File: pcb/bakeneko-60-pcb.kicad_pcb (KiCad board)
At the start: 2 copper layers, 284.7 x 94.2 mm, 147 parts, among them J1 JST SH 4-pin, J2 AVR-ISP-6, SW1 Reset, U1 SRV05-4, U2 ATmega32U4-AU, Y1 16MHz

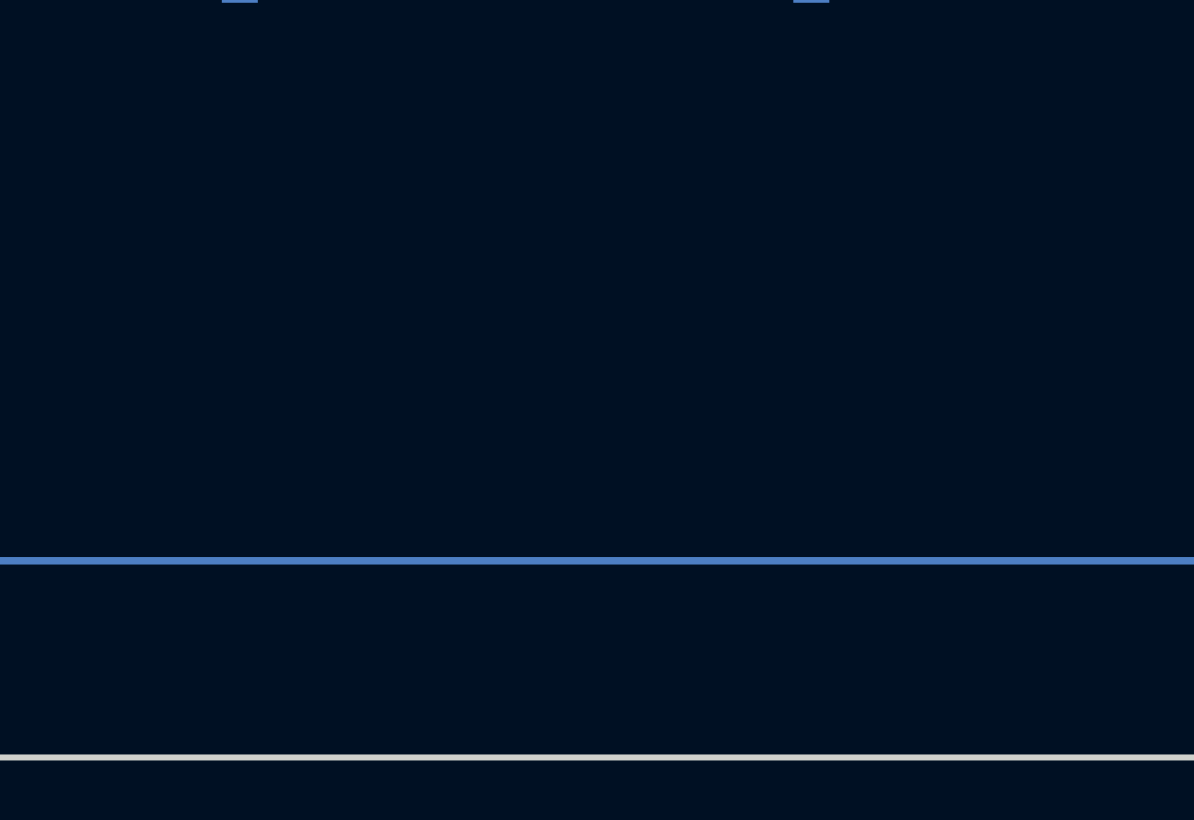
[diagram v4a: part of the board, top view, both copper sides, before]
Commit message: Place right 2.25 spacebar
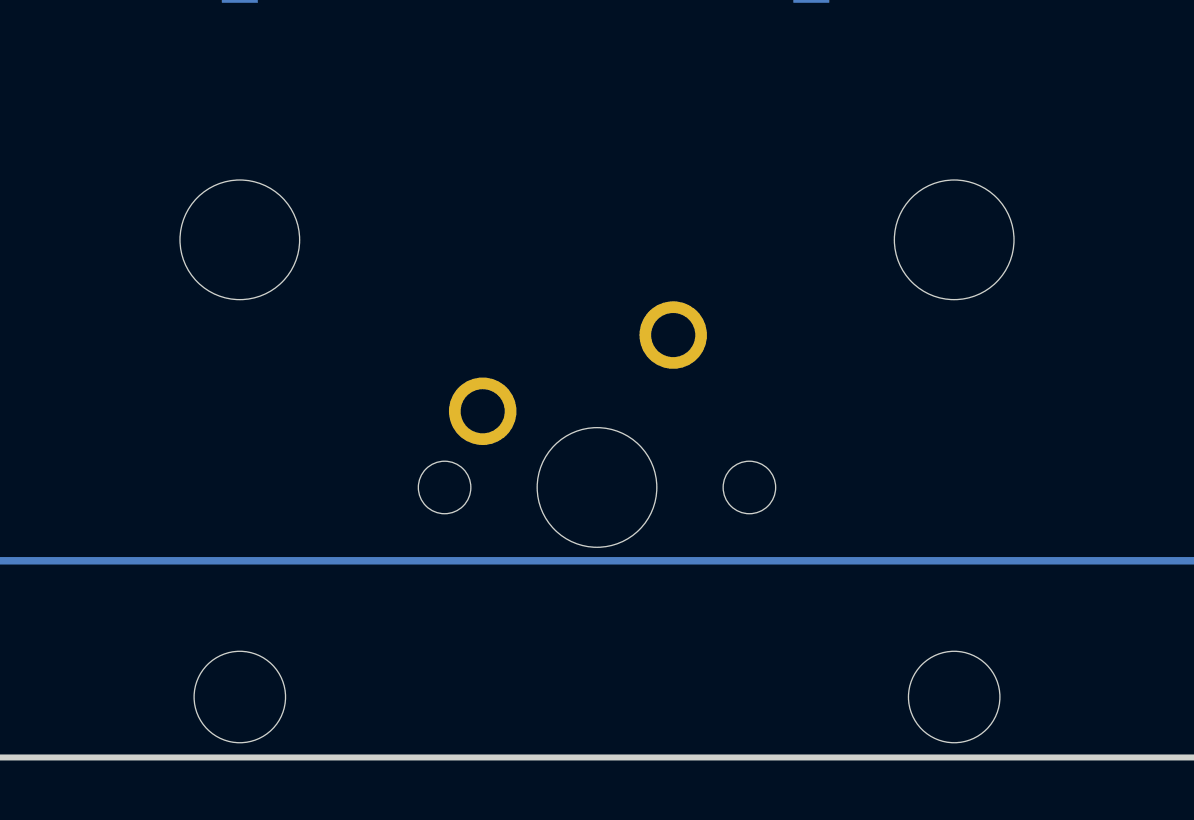
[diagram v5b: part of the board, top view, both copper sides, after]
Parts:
- added MX67: 2.25U, MX_Only:MXOnly-2.25U-ReversedStabilizers-NoLED, F.Cu at (168.5, 85.2)
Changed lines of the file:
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@@
       (net 91 "COL13"))
-  )
-  (footprint "MX_Only:MXOnly-2.25U-ReversedStabilizers-NoLED" (layer "F.Cu")
-    (at 92.34375 85.2)
-    (attr through_hole)
-    (fp_text reference "MX66" (at 0 3.175) (layer "Dwgs.User")
-      (effects (font (size 1 1) (thickness 0.15)))
-    )
-    (fp_text value "2.25U" (at 0 -7.9375) (layer "Dwgs.User")
-      (effects (font (size 1 1) (thickness 0.15)))
-    )
-    (fp_line (start 7 -7) (end 7 -5) (layer "Dwgs.User") (width 0.15))
-    (fp_line (start -7 -7) (end -7 -5) (layer "Dwgs.User") (width 0.15))
-    (fp_line (start 21.43125 -9.525) (end 21.43125 9.525) (layer "Dwgs.User") (width 0.15))
-    (fp_line (start -21.43125 9.525) (end -21.43125 -9.525) (layer "Dwgs.User") (width 0.15))
-    (fp_line (start 5 7) (end 7 7) (layer "Dwgs.User") (width 0.15))
-    (fp_line (start 7 7) (end 7 5) (layer "Dwgs.User") (width 0.15))
-    (fp_line (start -7 7) (end -5 7) (layer "Dwgs.User") (width 0.15))
-    (fp_line (start -21.43125 9.525) (end 21.43125 9.525) (layer "Dwgs.User") (width 0.15))
-    (fp_line (start -21.43125 -9.525) (end 21.43125 -9.525) (layer "Dwgs.User") (width 0.15))
-    (fp_line (start -7 5) (end -7 7) (layer "Dwgs.User") (width 0.15))
-    (fp_line (start 5 -7) (end 7 -7) (layer "Dwgs.User") (width 0.15))
-    (fp_line (start -5 -7) (end -7 -7) (layer "Dwgs.User") (width 0.15))
-    (pad "" np_thru_hole circle locked (at 0 0) (size 3.9878 3.9878) (drill 3.9878) (layers *.Cu *.Mask))
-    (pad "" np_thru_hole circle locked (at -11.90625 -8.255) (size 3.9878 3.9878) (drill 3.9878) (layers *.Cu *.Mask))
-    (pad "" np_thru_hole circle locked (at 5.08 0 48.0996) (size 1.75 1.75) (drill 1.75) (layers *.Cu *.Mask))
-    (pad "" np_thru_hole circle locked (at 11.90625 -8.255) (size 3.9878 3.9878) (drill 3.9878) (layers *.Cu *.Mask))
-    (pad "" np_thru_hole circle locked (at -11.90625 6.985) (size 3.048 3.048) (drill 3.048) (layers *.Cu *.Mask))
-    (pad "" np_thru_hole circle locked (at 11.90625 6.985) (size 3.048 3.048) (drill 3.048) (layers *.Cu *.Mask))
-    (pad "" np_thru_hole circle locked (at -5.08 0 48.0996) (size 1.75 1.75) (drill 1.75) (layers *.Cu *.Mask))
-    (pad "1" thru_hole circle locked (at -3.81 -2.54) (size 2.25 2.25) (drill 1.47) (layers *.Cu "B.Mask"))
-    (pad "2" thru_hole circle locked (at 2.54 -5.08) (size 2.25 2.25) (drill 1.47) (layers *.Cu "B.Mask"))
   )
   (footprint "MX_Only:MXOnly-1U-NoLED" (layer "F.Cu")
@@
       (net 92 "COL14"))
   )
+  (footprint "MX_Only:MXOnly-2.25U-ReversedStabilizers-NoLED" (layer "F.Cu")
+    (at 92.34375 85.2)
+    (attr through_hole)
+    (fp_text reference "MX66" (at 0 3.175) (layer "Dwgs.User")
+      (effects (font (size 1 1) (thickness 0.15)))
+    )
+    (fp_text value "2.25U" (at 0 -7.9375) (layer "Dwgs.User")
+      (effects (font (size 1 1) (thickness 0.15)))
+    )
+    (fp_line (start 7 -7) (end 7 -5) (layer "Dwgs.User") (width 0.15))
+    (fp_line (start -7 -7) (end -7 -5) (layer "Dwgs.User") (width 0.15))
+    (fp_line (start 21.43125 -9.525) (end 21.43125 9.525) (layer "Dwgs.User") (width 0.15))
+    (fp_line (start -21.43125 9.525) (end -21.43125 -9.525) (layer "Dwgs.User") (width 0.15))
+    (fp_line (start 5 7) (end 7 7) (layer "Dwgs.User") (width 0.15))
+    (fp_line (start 7 7) (end 7 5) (layer "Dwgs.User") (width 0.15))
+    (fp_line (start -7 7) (end -5 7) (layer "Dwgs.User") (width 0.15))
+    (fp_line (start -21.43125 9.525) (end 21.43125 9.525) (layer "Dwgs.User") (width 0.15))
+    (fp_line (start -21.43125 -9.525) (end 21.43125 -9.525) (layer "Dwgs.User") (width 0.15))
+    (fp_line (start -7 5) (end -7 7) (layer "Dwgs.User") (width 0.15))
+    (fp_line (start 5 -7) (end 7 -7) (layer "Dwgs.User") (width 0.15))
+    (fp_line (start -5 -7) (end -7 -7) (layer "Dwgs.User") (width 0.15))
+    (pad "" np_thru_hole circle locked (at 0 0) (size 3.9878 3.9878) (drill 3.9878) (layers *.Cu *.Mask))
+    (pad "" np_thru_hole circle locked (at -11.90625 -8.255) (size 3.9878 3.9878) (drill 3.9878) (layers *.Cu *.Mask))
+    (pad "" np_thru_hole circle locked (at 5.08 0 48.0996) (size 1.75 1.75) (drill 1.75) (layers *.Cu *.Mask))
+    (pad "" np_thru_hole circle locked (at 11.90625 -8.255) (size 3.9878 3.9878) (drill 3.9878) (layers *.Cu *.Mask))
+    (pad "" np_thru_hole circle locked (at -11.90625 6.985) (size 3.048 3.048) (drill 3.048) (layers *.Cu *.Mask))
+    (pad "" np_thru_hole circle locked (at 11.90625 6.985) (size 3.048 3.048) (drill 3.048) (layers *.Cu *.Mask))
+    (pad "" np_thru_hole circle locked (at -5.08 0 48.0996) (size 1.75 1.75) (drill 1.75) (layers *.Cu *.Mask))
+    (pad "1" thru_hole circle locked (at -3.81 -2.54) (size 2.25 2.25) (drill 1.47) (layers *.Cu "B.Mask"))
+    (pad "2" thru_hole circle locked (at 2.54 -5.08) (size 2.25 2.25) (drill 1.47) (layers *.Cu "B.Mask"))
+  )
+  (footprint "MX_Only:MXOnly-2.25U-ReversedStabilizers-NoLED" (layer "F.Cu")
+    (at 168.54375 85.2)
+    (attr through_hole)
+    (fp_text reference "MX67" (at 0 3.175) (layer "Dwgs.User")
+      (effects (font (size 1 1) (thickness 0.15)))
+    )
+    (fp_text value "2.25U" (at 0 -7.9375) (layer "Dwgs.User")
+      (effects (font (size 1 1) (thickness 0.15)))
+    )
+    (fp_line (start -7 -7) (end -7 -5) (layer "Dwgs.User") (width 0.15))
+    (fp_line (start 7 7) (end 7 5) (layer "Dwgs.User") (width 0.15))
+    (fp_line (start -7 7) (end -5 7) (layer "Dwgs.User") (width 0.15))
+    (fp_line (start 21.43125 -9.525) (end 21.43125 9.525) (layer "Dwgs.User") (width 0.15))
+    (fp_line (start 7 -7) (end 7 -5) (layer "Dwgs.User") (width 0.15))
+    (fp_line (start 5 -7) (end 7 -7) (layer "Dwgs.User") (width 0.15))
+    (fp_line (start -21.43125 9.525) (end -21.43125 -9.525) (layer "Dwgs.User") (width 0.15))
+    (fp_line (start 5 7) (end 7 7) (layer "Dwgs.User") (width 0.15))
+    (fp_line (start -5 -7) (end -7 -7) (layer "Dwgs.User") (width 0.15))
+    (fp_line (start -7 5) (end -7 7) (layer "Dwgs.User") (width 0.15))
+    (fp_line (start -21.43125 -9.525) (end 21.43125 -9.525) (layer "Dwgs.User") (width 0.15))
+    (fp_line (start -21.43125 9.525) (end 21.43125 9.525) (layer "Dwgs.User") (width 0.15))
+    (pad "" np_thru_hole circle locked (at 0 0) (size 3.9878 3.9878) (drill 3.9878) (layers *.Cu *.Mask))
+    (pad "" np_thru_hole circle locked (at -11.90625 -8.255) (size 3.9878 3.9878) (drill 3.9878) (layers *.Cu *.Mask))
+    (pad "" np_thru_hole circle locked (at -5.08 0 48.0996) (size 1.75 1.75) (drill 1.75) (layers *.Cu *.Mask))
+    (pad "" np_thru_hole circle locked (at 11.90625 -8.255) (size 3.9878 3.9878) (drill 3.9878) (layers *.Cu *.Mask))
+    (pad "" np_thru_hole circle locked (at 5.08 0 48.0996) (size 1.75 1.75) (drill 1.75) (layers *.Cu *.Mask))
+    (pad "" np_thru_hole circle locked (at 11.90625 6.985) (size 3.048 3.048) (drill 3.048) (layers *.Cu *.Mask))
+    (pad "" np_thru_hole circle locked (at -11.90625 6.985) (size 3.048 3.048) (drill 3.048) (layers *.Cu *.Mask))
+    (pad "1" thru_hole circle locked (at -3.81 -2.54) (size 2.25 2.25) (drill 1.47) (layers *.Cu "B.Mask"))
+    (pad "2" thru_hole circle locked (at 2.54 -5.08) (size 2.25 2.25) (drill 1.47) (layers *.Cu "B.Mask"))
+  )
   (footprint "Fuse:Fuse_1206_3216Metric" (layer "B.Cu")

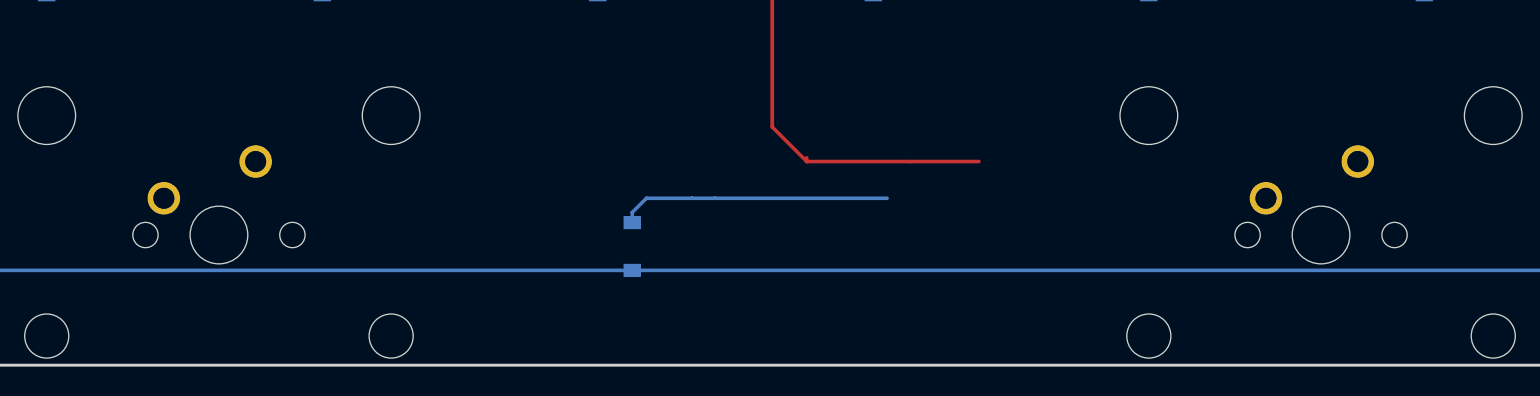
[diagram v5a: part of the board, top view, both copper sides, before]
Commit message: Add left and right 2.75u spacebars
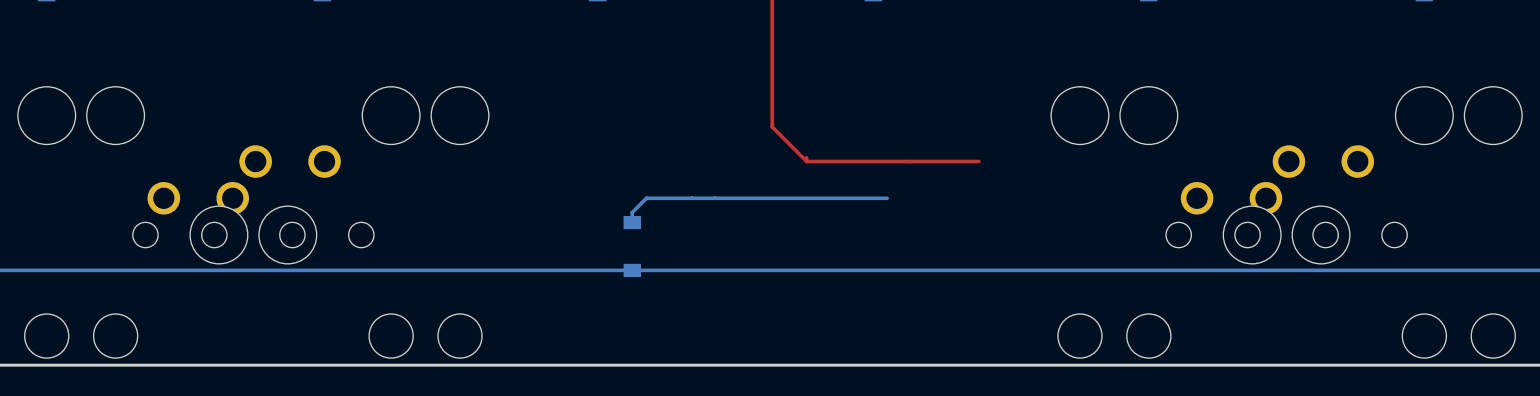
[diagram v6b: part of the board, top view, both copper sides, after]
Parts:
- added REF**: 2.75U, MX_Only:MXOnly-2.75U-ReversedStabilizers-NoLED, F.Cu at (97.1, 85.2)
- added REF**: 2.75U, MX_Only:MXOnly-2.75U-ReversedStabilizers-NoLED, F.Cu at (163.8, 85.2)
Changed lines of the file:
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@@
+    (pad "2" thru_hole circle locked (at 2.54 -5.08) (size 2.25 2.25) (drill 1.47) (layers *.Cu "B.Mask"))
+  )
+  (footprint "MX_Only:MXOnly-2.75U-ReversedStabilizers-NoLED" (layer "F.Cu")
+    (at 97.10625 85.2)
+    (attr through_hole)
+    (fp_text reference "REF**" (at 0 3.175) (layer "Dwgs.User")
+      (effects (font (size 1 1) (thickness 0.15)))
+    )
+    (fp_text value "2.75U" (at 0 -7.9375) (layer "Dwgs.User")
+      (effects (font (size 1 1) (thickness 0.15)))
+    )
+    (fp_line (start -7 5) (end -7 7) (layer "Dwgs.User") (width 0.15))
+    (fp_line (start 5 -7) (end 7 -7) (layer "Dwgs.User") (width 0.15))
+    (fp_line (start 7 7) (end 7 5) (layer "Dwgs.User") (width 0.15))
+    (fp_line (start -7 -7) (end -7 -5) (layer "Dwgs.User") (width 0.15))
+    (fp_line (start -26.19375 9.525) (end 26.19375 9.525) (layer "Dwgs.User") (width 0.15))
+    (fp_line (start 7 -7) (end 7 -5) (layer "Dwgs.User") (width 0.15))
+    (fp_line (start -26.19375 -9.525) (end 26.19375 -9.525) (layer "Dwgs.User") (width 0.15))
+    (fp_line (start -26.19375 9.525) (end -26.19375 -9.525) (layer "Dwgs.User") (width 0.15))
+    (fp_line (start -7 7) (end -5 7) (layer "Dwgs.User") (width 0.15))
+    (fp_line (start 26.19375 -9.525) (end 26.19375 9.525) (layer "Dwgs.User") (width 0.15))
+    (fp_line (start 5 7) (end 7 7) (layer "Dwgs.User") (width 0.15))
+    (fp_line (start -5 -7) (end -7 -7) (layer "Dwgs.User") (width 0.15))
+    (pad "" np_thru_hole circle locked (at -11.90625 -8.255) (size 3.9878 3.9878) (drill 3.9878) (layers *.Cu *.Mask))
+    (pad "" np_thru_hole circle locked (at 5.08 0 48.0996) (size 1.75 1.75) (drill 1.75) (layers *.Cu *.Mask))
+    (pad "" np_thru_hole circle locked (at 11.90625 -8.255) (size 3.9878 3.9878) (drill 3.9878) (layers *.Cu *.Mask))
+    (pad "" np_thru_hole circle locked (at 11.90625 6.985) (size 3.048 3.048) (drill 3.048) (layers *.Cu *.Mask))
+    (pad "" np_thru_hole circle locked (at -11.90625 6.985) (size 3.048 3.048) (drill 3.048) (layers *.Cu *.Mask))
+    (pad "" np_thru_hole circle locked (at 0 0) (size 3.9878 3.9878) (drill 3.9878) (layers *.Cu *.Mask))
+    (pad "" np_thru_hole circle locked (at -5.08 0 48.0996) (size 1.75 1.75) (drill 1.75) (layers *.Cu *.Mask))
+    (pad "1" thru_hole circle locked (at -3.81 -2.54) (size 2.25 2.25) (drill 1.47) (layers *.Cu "B.Mask"))
+    (pad "2" thru_hole circle locked (at 2.54 -5.08) (size 2.25 2.25) (drill 1.47) (layers *.Cu "B.Mask"))
+  )
+  (footprint "MX_Only:MXOnly-2.75U-ReversedStabilizers-NoLED" (layer "F.Cu")
+    (at 163.78125 85.2)
+    (attr through_hole)
+    (fp_text reference "REF**" (at 0 3.175) (layer "Dwgs.User")
+      (effects (font (size 1 1) (thickness 0.15)))
+    )
+    (fp_text value "2.75U" (at 0 -7.9375) (layer "Dwgs.User")
+      (effects (font (size 1 1) (thickness 0.15)))
+    )
+    (fp_line (start 5 7) (end 7 7) (layer "Dwgs.User") (width 0.15))
+    (fp_line (start -7 5) (end -7 7) (layer "Dwgs.User") (width 0.15))
+    (fp_line (start -26.19375 9.525) (end -26.19375 -9.525) (layer "Dwgs.User") (width 0.15))
+    (fp_line (start -7 -7) (end -7 -5) (layer "Dwgs.User") (width 0.15))
+    (fp_line (start 7 7) (end 7 5) (layer "Dwgs.User") (width 0.15))
+    (fp_line (start 7 -7) (end 7 -5) (layer "Dwgs.User") (width 0.15))
+    (fp_line (start 26.19375 -9.525) (end 26.19375 9.525) (layer "Dwgs.User") (width 0.15))
+    (fp_line (start -26.19375 9.525) (end 26.19375 9.525) (layer "Dwgs.User") (width 0.15))
+    (fp_line (start -26.19375 -9.525) (end 26.19375 -9.525) (layer "Dwgs.User") (width 0.15))
+    (fp_line (start -5 -7) (end -7 -7) (layer "Dwgs.User") (width 0.15))
+    (fp_line (start -7 7) (end -5 7) (layer "Dwgs.User") (width 0.15))
+    (fp_line (start 5 -7) (end 7 -7) (layer "Dwgs.User") (width 0.15))
+    (pad "" np_thru_hole circle locked (at 5.08 0 48.0996) (size 1.75 1.75) (drill 1.75) (layers *.Cu *.Mask))
+    (pad "" np_thru_hole circle locked (at 11.90625 6.985) (size 3.048 3.048) (drill 3.048) (layers *.Cu *.Mask))
+    (pad "" np_thru_hole circle locked (at -5.08 0 48.0996) (size 1.75 1.75) (drill 1.75) (layers *.Cu *.Mask))
+    (pad "" np_thru_hole circle locked (at 0 0) (size 3.9878 3.9878) (drill 3.9878) (layers *.Cu *.Mask))
+    (pad "" np_thru_hole circle locked (at -11.90625 -8.255) (size 3.9878 3.9878) (drill 3.9878) (layers *.Cu *.Mask))
+    (pad "" np_thru_hole circle locked (at -11.90625 6.985) (size 3.048 3.048) (drill 3.048) (layers *.Cu *.Mask))
+    (pad "" np_thru_hole circle locked (at 11.90625 -8.255) (size 3.9878 3.9878) (drill 3.9878) (layers *.Cu *.Mask))
+    (pad "1" thru_hole circle locked (at -3.81 -2.54) (size 2.25 2.25) (drill 1.47) (layers *.Cu "B.Mask"))
     (pad "2" thru_hole circle locked (at 2.54 -5.08) (size 2.25 2.25) (drill 1.47) (layers *.Cu "B.Mask"))
   )

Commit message: Add middle 1.25 keys and cleanup unused traces/diodes
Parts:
- removed D59: 1N4148, Diode_SMD:D_SOD-123
- added MX70: 1.25U, MX_Only:MXOnly-1.25U-NoLED, F.Cu at (125.7, 85.2)
- added MX71: 1.25U, MX_Only:MXOnly-1.25U-NoLED, F.Cu at (135.2, 85.2)
- renumbered REF** to MX68, REF** to MX69
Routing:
- net COL6: track 212.3 -> 180.1 mm
- net Net-(D59-Pad2): track 18.7 -> 0.00 mm
- net Net-(D58-Pad2): track 9.20 -> 6.82 mm
- net Net-(D57-Pad2): track 9.20 -> 6.82 mm
- net COL13: track 351.9 -> 349.5 mm
- net COL12: track 325.5 -> 323.1 mm

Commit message: Renumber switches
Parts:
- renumbered MX66 to MX62, MX68 to MX63, MX70 to MX64, MX71 to MX65, MX69 to MX66, MX62 to MX68, MX63 to MX69, MX64 to MX70, MX65 to MX71
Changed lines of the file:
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@@
     (at 201.88125 85.2)
     (attr through_hole)
-    (fp_text reference "MX62" (at 0 3.175) (layer "Dwgs.User")
+    (fp_text reference "MX68" (at 0 3.175) (layer "Dwgs.User")
       (effects (font (size 1 1) (thickness 0.15)))
     )
@@
     (at 225.69375 85.2)
     (attr through_hole)
-    (fp_text reference "MX63" (at 0 3.175) (layer "Dwgs.User")
+    (fp_text reference "MX69" (at 0 3.175) (layer "Dwgs.User")
       (effects (font (size 1 1) (thickness 0.15)))
     )
@@
     (at 249.50625 85.2)
     (attr through_hole)
-    (fp_text reference "MX64" (at 0 3.175) (layer "Dwgs.User")
+    (fp_text reference "MX70" (at 0 3.175) (layer "Dwgs.User")
       (effects (font (size 1 1) (thickness 0.15)))
     )
@@
     (at 273.31875 85.2)
     (attr through_hole)
-    (fp_text reference "MX65" (at 0 3.175) (layer "Dwgs.User")
+    (fp_text reference "MX71" (at 0 3.175) (layer "Dwgs.User")
       (effects (font (size 1 1) (thickness 0.15)))
     )
@@
     (at 92.34375 85.2)
     (attr through_hole)
-    (fp_text reference "MX66" (at 0 3.175) (layer "Dwgs.User")
+    (fp_text reference "MX62" (at 0 3.175) (layer "Dwgs.User")
       (effects (font (size 1 1) (thickness 0.15)))
     )
@@
     (at 97.10625 85.2)
     (attr through_hole)
-    (fp_text reference "MX68" (at 0 3.175) (layer "Dwgs.User")
+    (fp_text reference "MX63" (at 0 3.175) (layer "Dwgs.User")
       (effects (font (size 1 1) (thickness 0.15)))
     )
@@
     (at 125.68125 85.2)
     (attr through_hole)
-    (fp_text reference "MX70" (at 0 3.175) (layer "Dwgs.User")
+    (fp_text reference "MX64" (at 0 3.175) (layer "Dwgs.User")
       (effects (font (size 1 1) (thickness 0.15)))
     )
@@
     (at 135.20625 85.2)
     (attr through_hole)
-    (fp_text reference "MX71" (at 0 3.175) (layer "Dwgs.User")
+    (fp_text reference "MX65" (at 0 3.175) (layer "Dwgs.User")
       (effects (font (size 1 1) (thickness 0.15)))
     )
@@
     (at 163.78125 85.2)
     (attr through_hole)
-    (fp_text reference "MX69" (at 0 3.175) (layer "Dwgs.User")
-      (effects (font (size 1 1) (thickness 0.15)))
-    )
+    (fp_text reference "MX66" (at 0 3.175) (layer "Dwgs.User")
+      (effects (font (size 1 1) (thickness 0.15)))
+    )
